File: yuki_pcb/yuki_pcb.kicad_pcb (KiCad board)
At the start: 2 copper layers, 142 x 98 mm, 25 parts, among them J1 TRRS, K00 KEYSW, K01 KEYSW, K02 KEYSW, K03 KEYSW, K04 KEYSW, K05 KEYSW, K10 KEYSW, K11 KEYSW, K12 KEYSW, K13 KEYSW, K14 KEYSW, K15 KEYSW, K20 KEYSW, K21 KEYSW, K22 KEYSW, K23 KEYSW, K24 KEYSW, K25 KEYSW, K30 KEYSW, K31 KEYSW, K32 KEYSW, K33 KEYSW, U1 YAAJ_WeAct_BlackPill_Part_Like

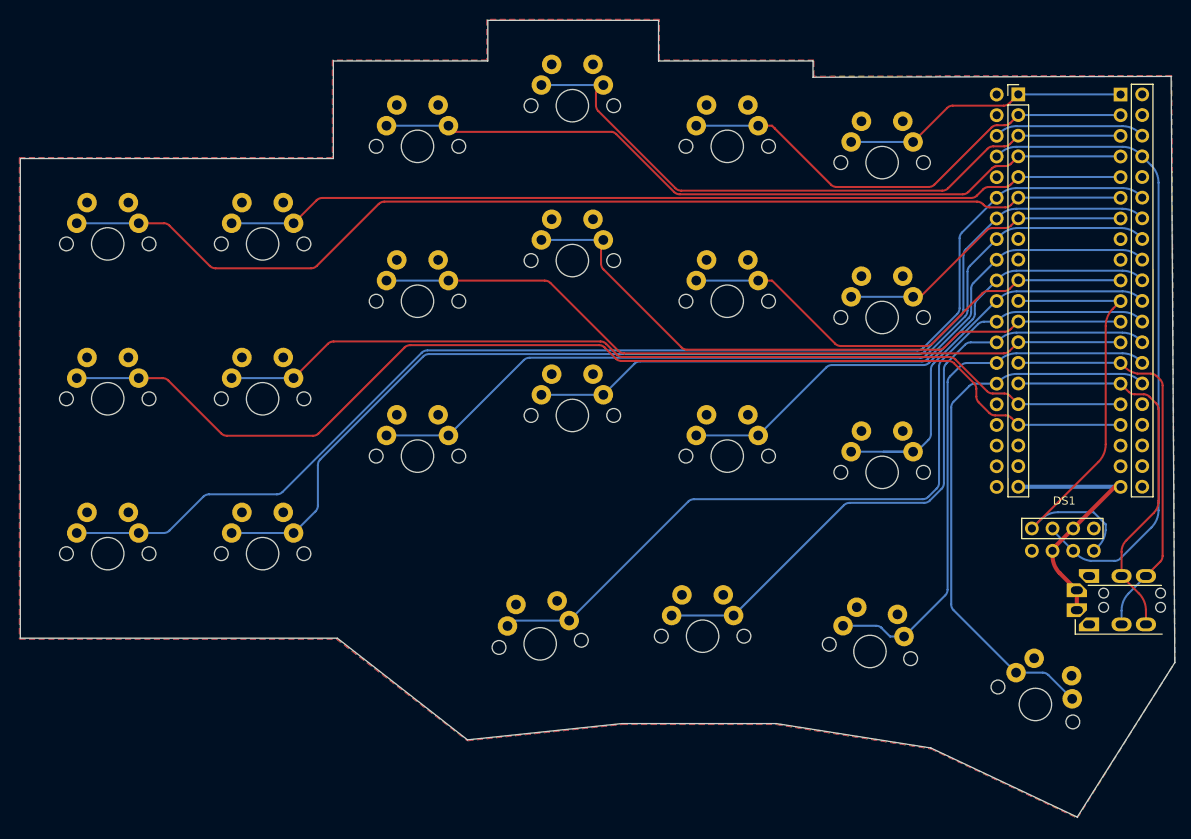
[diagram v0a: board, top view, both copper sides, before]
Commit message: rounded edges
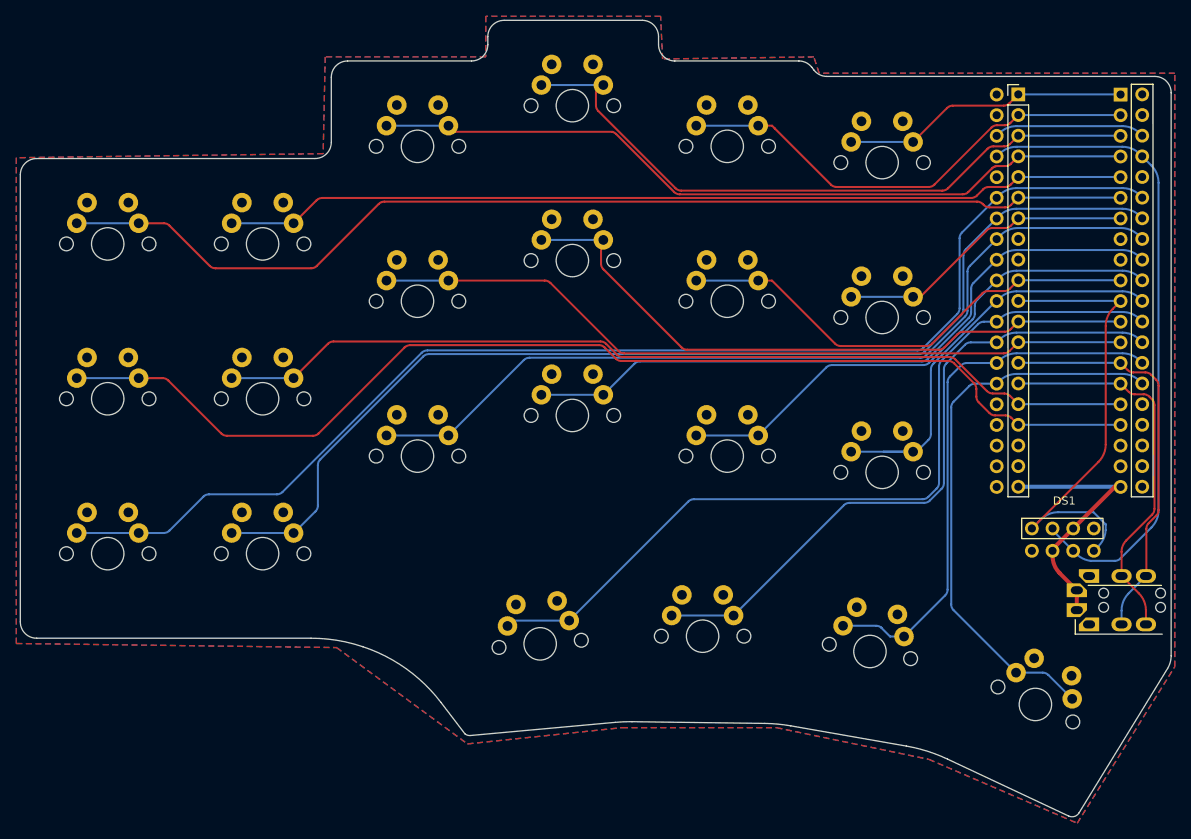
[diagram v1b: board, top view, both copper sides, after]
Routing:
- net /TX: track 50.2 -> 49.5 mm
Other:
- board size 142 x 98 mm -> 141.6 x 98 mm

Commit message: more silksreen
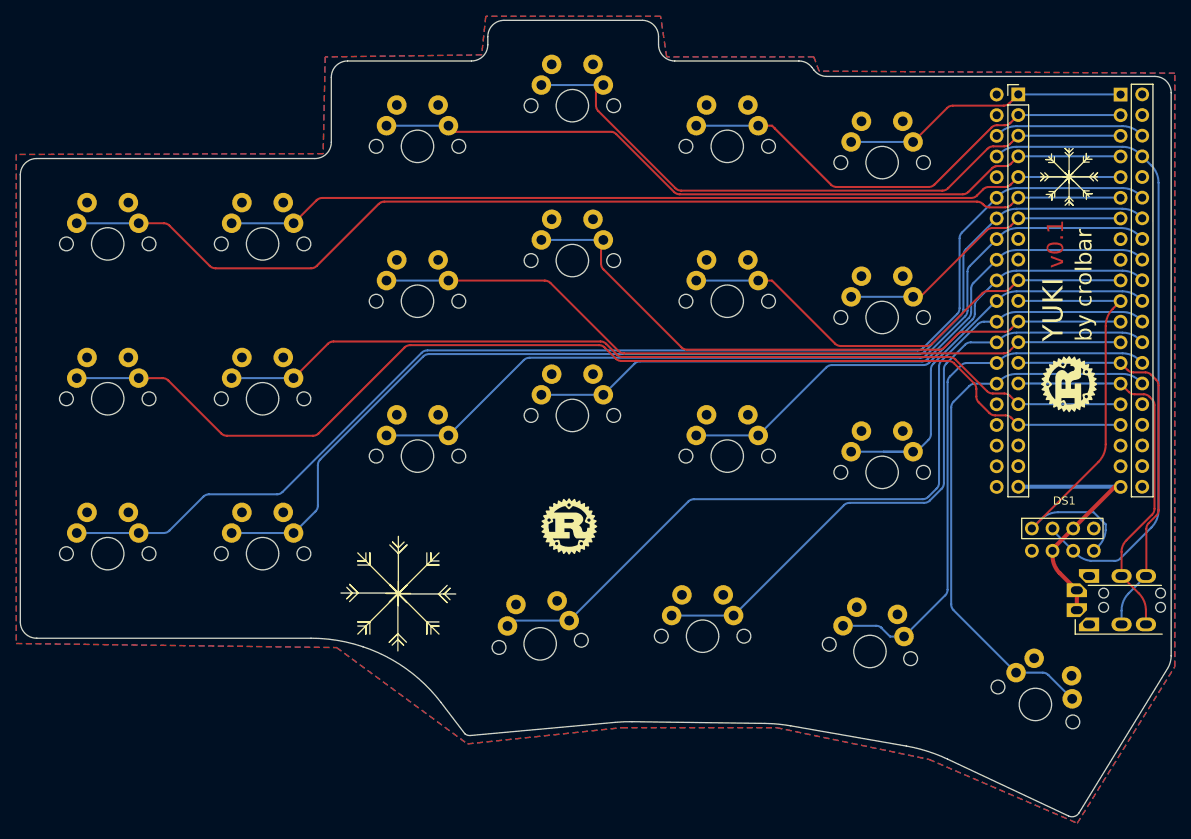
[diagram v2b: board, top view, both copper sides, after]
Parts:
- added G***: LOGO, YUKI:RUST_GEAR, F.Cu at (187.0, 87.2)
- added G***: LOGO, YUKI:RUST_GEAR, F.Cu at (125.5, 104.8)
- added G***: LOGO, YUKI:RUST_GEAR, B.Cu at (125.5, 104.8)
- added REF**: SNOWFLAKE_SMALL, YUKI:SNOWFLAKE_SMALL, F.Cu at (187.0, 61.8)
- added REF**: SNOWFLAKE, YUKI:SNOWFLAKE, F.Cu at (104.5, 113.0)
- added REF**: SNOWFLAKE, YUKI:SNOWFLAKE, B.Cu at (104.5, 113.0)
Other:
- board text added: "YUKI"
- board text added: "by crolbar"
- board text added: "v0.1"

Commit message: some firmware
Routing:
- net /k04: track 58.8 -> 59.5 mm

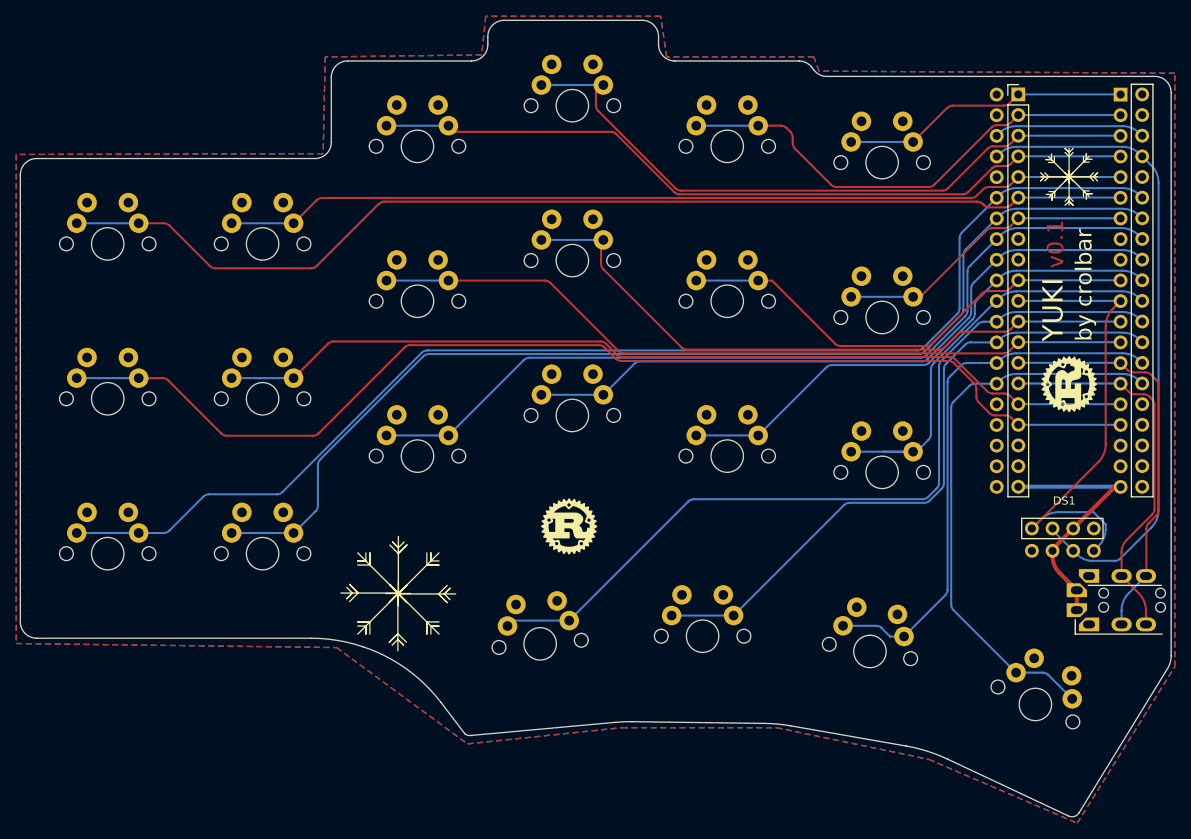
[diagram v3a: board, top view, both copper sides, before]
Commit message: v0.2 with Choc switches!
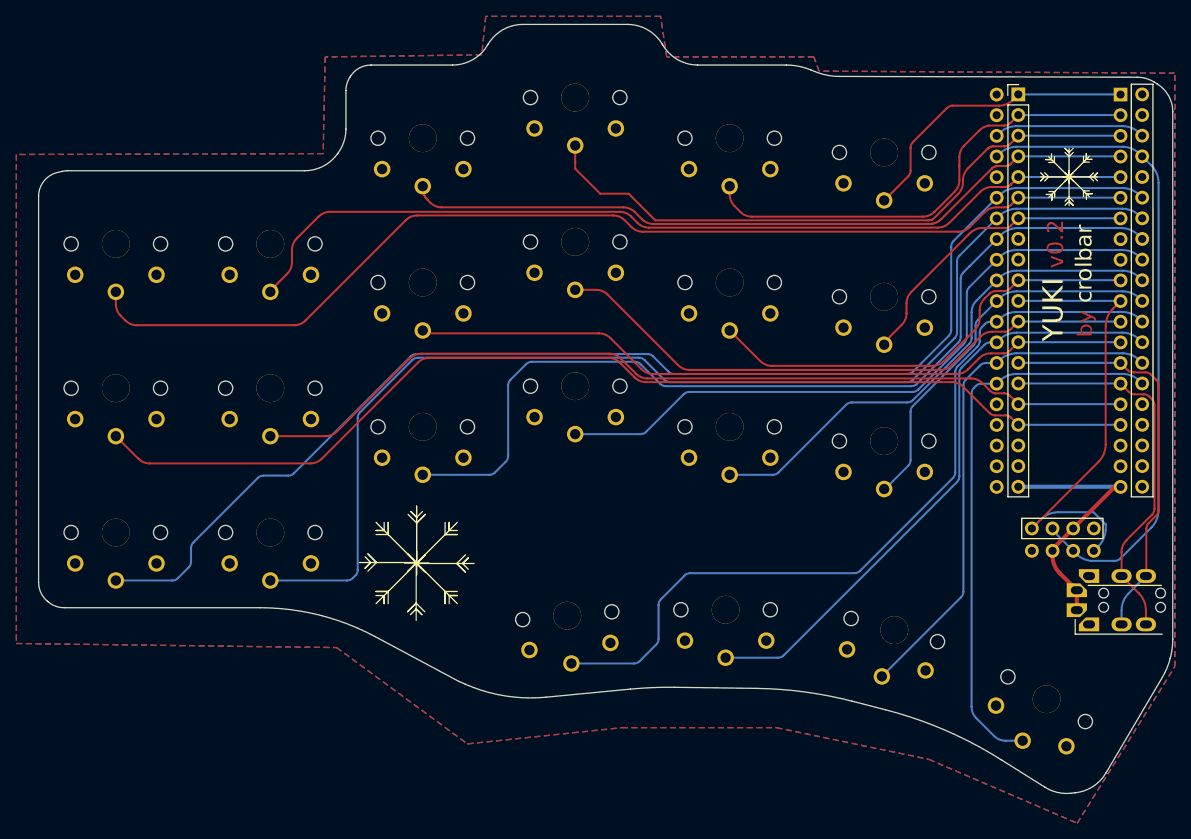
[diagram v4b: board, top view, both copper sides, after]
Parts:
- removed G*** (x3): LOGO, YUKI:RUST_GEAR
- K00, K01, K02, K03, K04, K05, K10, K11, K12, K13, K14, K15, K20, K21, K22, K23, K24, K25, K30, K31, K32, K33: footprint YUKI:CherryMX_rev -> YUKI:Kailh_Choc_PG1350_rev
- moved K30 4.81 mm to (125.3, 115.7)
- moved REF** 4.37 mm to (106.8, 109.2) (x2)
- moved K31 4.31 mm to (144.8, 115.0)
- moved K32 3.99 mm to (165.5, 117.5), turned to -15 degrees
- moved K25 3.86 mm to (164.2, 94.2)
- moved K22 3.66 mm to (107.5, 92.5)
- moved K23 3.62 mm to (126.2, 87.5)
- moved K24 3.61 mm to (145.2, 92.5)
- moved K20 2.79 mm to (69.8, 105.5)
- moved K21 2.77 mm to (88.8, 105.5)
- moved K15 2.56 mm to (164.2, 76.5)
- moved K12 2.39 mm to (107.5, 74.8)
- moved K13 2.33 mm to (126.2, 69.8)
- moved K14 2.32 mm to (145.2, 74.8)
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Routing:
- net /k21: track 137.0 -> 146.2 mm
- net /k10: track 140.5 -> 133.1 mm
- net /k13: track 80.3 -> 73.2 mm
- net /k22: track 107.7 -> 114.4 mm
- net /k25: track 53.6 -> 48.2 mm
- net /k31: track 81.7 -> 76.5 mm
- net /k12: track 94.4 -> 89.2 mm
- net /k03: track 82.2 -> 77.7 mm
- net /k02: track 95.5 -> 91.3 mm
- net /k32: track 68.2 -> 64.7 mm
- net /k14: track 58.7 -> 55.3 mm
- net /k30: track 103.7 -> 100.3 mm
- net /k11: track 114.1 -> 110.8 mm
- net /k01: track 111.5 -> 113.3 mm
- net /k04: track 59.5 -> 58.1 mm
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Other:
- board size 141.6 x 98 mm -> 139.5 x 94.6 mm
- board text added: "by"
- board text added: "crolbar"
- board text added: "v0.2"
- board text removed: "DS1"
- board text removed: "by crolbar"
- board text removed: "v0.1"
